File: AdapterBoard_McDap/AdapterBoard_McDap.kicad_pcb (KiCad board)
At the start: 2 copper layers, 5 parts, among them J1 CN7, J2 CN10, J2_J4 LaunchPad, J3_J1 LaunchPad, J5 RSLK2

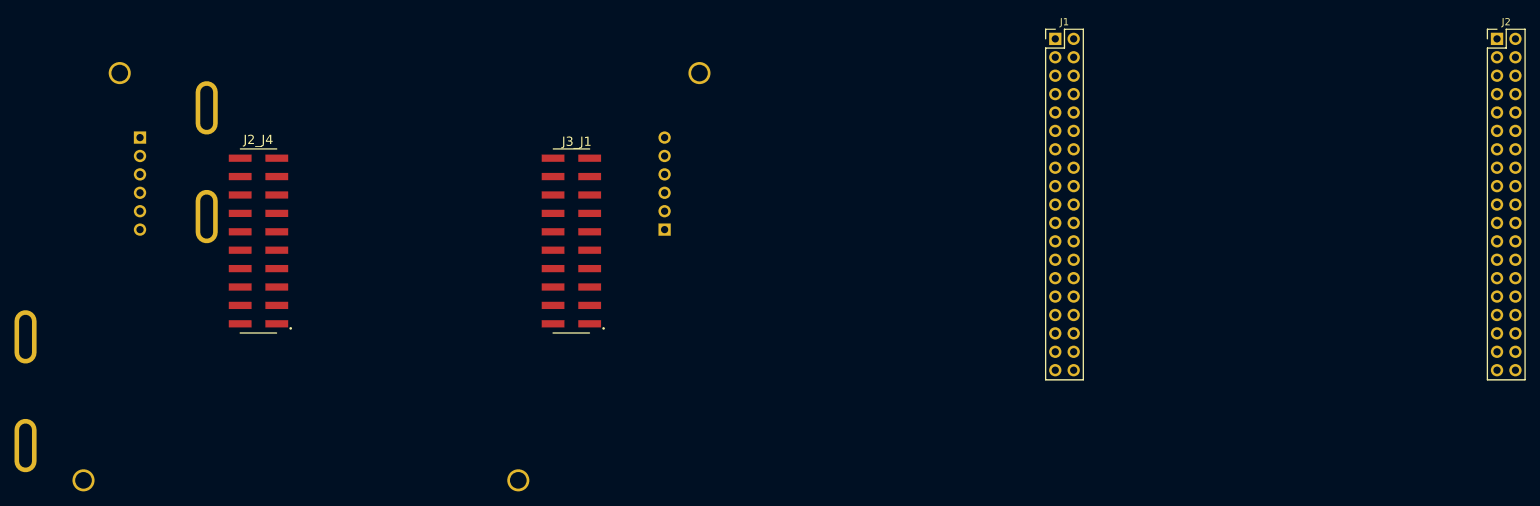
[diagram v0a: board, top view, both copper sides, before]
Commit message: Added pinmap connections to schematic; Finished layout for adapter board
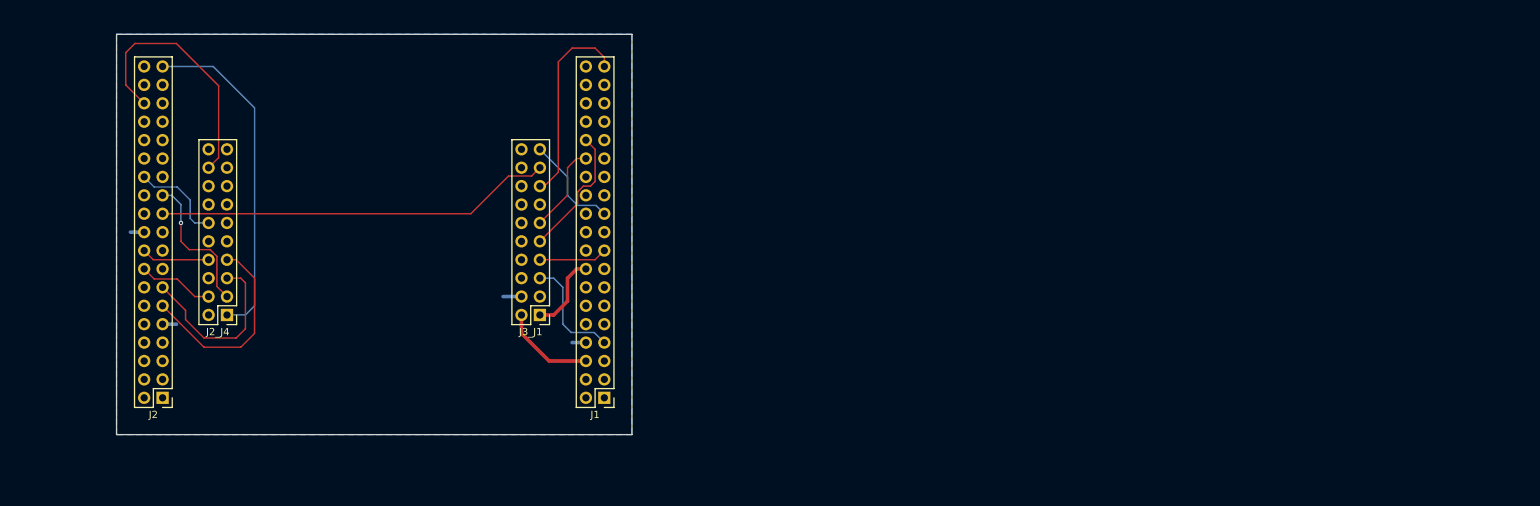
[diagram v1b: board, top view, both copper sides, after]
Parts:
- J2_J4, J3_J1: footprint RSLK2:LaunchPad -> Connector_PinHeader_2.54mm:PinHeader_2x10_P2.54mm_Vertical
- moved J2 190.7 mm to (67.3, 130.8), turned to 180 degrees
- moved J1 79.5 mm to (128.3, 130.8), turned to 180 degrees
- moved J2_J4 11.1 mm to (76.2, 119.4), turned to 180 degrees
- moved J3_J1 11.1 mm to (119.4, 119.4), turned to 180 degrees
- moved J5 5.75 mm to (50.8, 141.0)
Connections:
- J1 pad 17: PA_15 -> PA8
- J1 pad 21: PB_7 -> PB3
- J1 pad 30: PA_1 -> PA26
- J1 pad 37: PC_3 -> PA27
- J1 pad 6: E5V -> +5V
- J1 pad 7: PA_14 -> PA9
- J2 pad 11: PA_5 -> PA31
- J2 pad 13: PA_6 -> PA28
- J2 pad 16: PC_1 -> PB12
- J2 pad 18: PC_0 -> PB15
- J2 pad 26: PB_15 -> PB8
- J2 pad 37: PC_5 -> PB4
- J2_J4 pad 18: PB0 -> PA_2
- J2_J4 pad 3: PB1 -> PA_8
- J3_J1 pad 1: /LP3_3 -> 3V3
- J3_J1 pad 11: PB24 -> PA_0
- J3_J1 pad 17: PB2 -> PA_9
- J3_J1 pad 2: /VBUS -> +5V
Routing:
- net PA_9: track 0.00 -> 54.7 mm
- net PB4: track 0.00 -> 46.7 mm
- net PA_2: track 0.00 -> 35.7 mm
- net PA31: track 0.00 -> 28.3 mm
- net PA27: track 0.00 -> 27.5 mm
- net PA28: track 0.00 -> 24.7 mm
- net PA_8: track 0.00 -> 20.1 mm, vias 0 -> 1
- net PA26: track 0.00 -> 18.2 mm
- net PA9: track 0.00 -> 15.5 mm
- net PB3: track 0.00 -> 14.1 mm
- net PB8: track 0.00 -> 13.0 mm
- net +5V: track 0.00 -> 13.0 mm
- net PA_0: track 0.00 -> 12.3 mm
- net 3V3: track 0.00 -> 10.8 mm
- net PB12: track 0.00 -> 10.5 mm
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- added copper zone on B.Cu, net GND
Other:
- board outline added: 71.1 x 55.2 mm
